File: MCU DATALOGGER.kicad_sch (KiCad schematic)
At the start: 0 parts

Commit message: Setup of EEschema for new project
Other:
- title: (none) -> MCU DATALOGGER
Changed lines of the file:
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@@
 	(generator_version "9.0")
 	(paper "A4")
+	(title_block
+		(title "MCU DATALOGGER")
+		(date "2026-05-03")
+		(rev "1")
+	)
 	(sheet_instances
 		(path "/"

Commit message: Have added required symbols to the schematic sheets
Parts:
- added BT1: Battery, symbol Device:Battery
- added C1, C2, C3, C4: C, symbol Device:C
- added C5: C_Polarized, symbol Device:C_Polarized
- added D1, D2: LED, symbol Device:LED
- added H1, H2, H3, H4, H5: MountingHole, symbol Mechanical:MountingHole
- added R1, R2, R3, R4, R5, R6, R7: R, symbol Device:R
- added U1, U2: 24LC1025, symbol Memory_EEPROM:24LC1025
- added U3: ATMEGA328P-AU, digikey-footprints:TQFP-32_7x7mm, symbol dk_Embedded-Microcontrollers:ATMEGA328P-AU
- added U4: DS1337S_, DS1337S_:SOIC127P600X175-8N, symbol DS1337S_:DS1337S_
- added Y1, Y2: Crystal, symbol Device:Crystal
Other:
- added sheet connectors (connectors.kicad_sch)

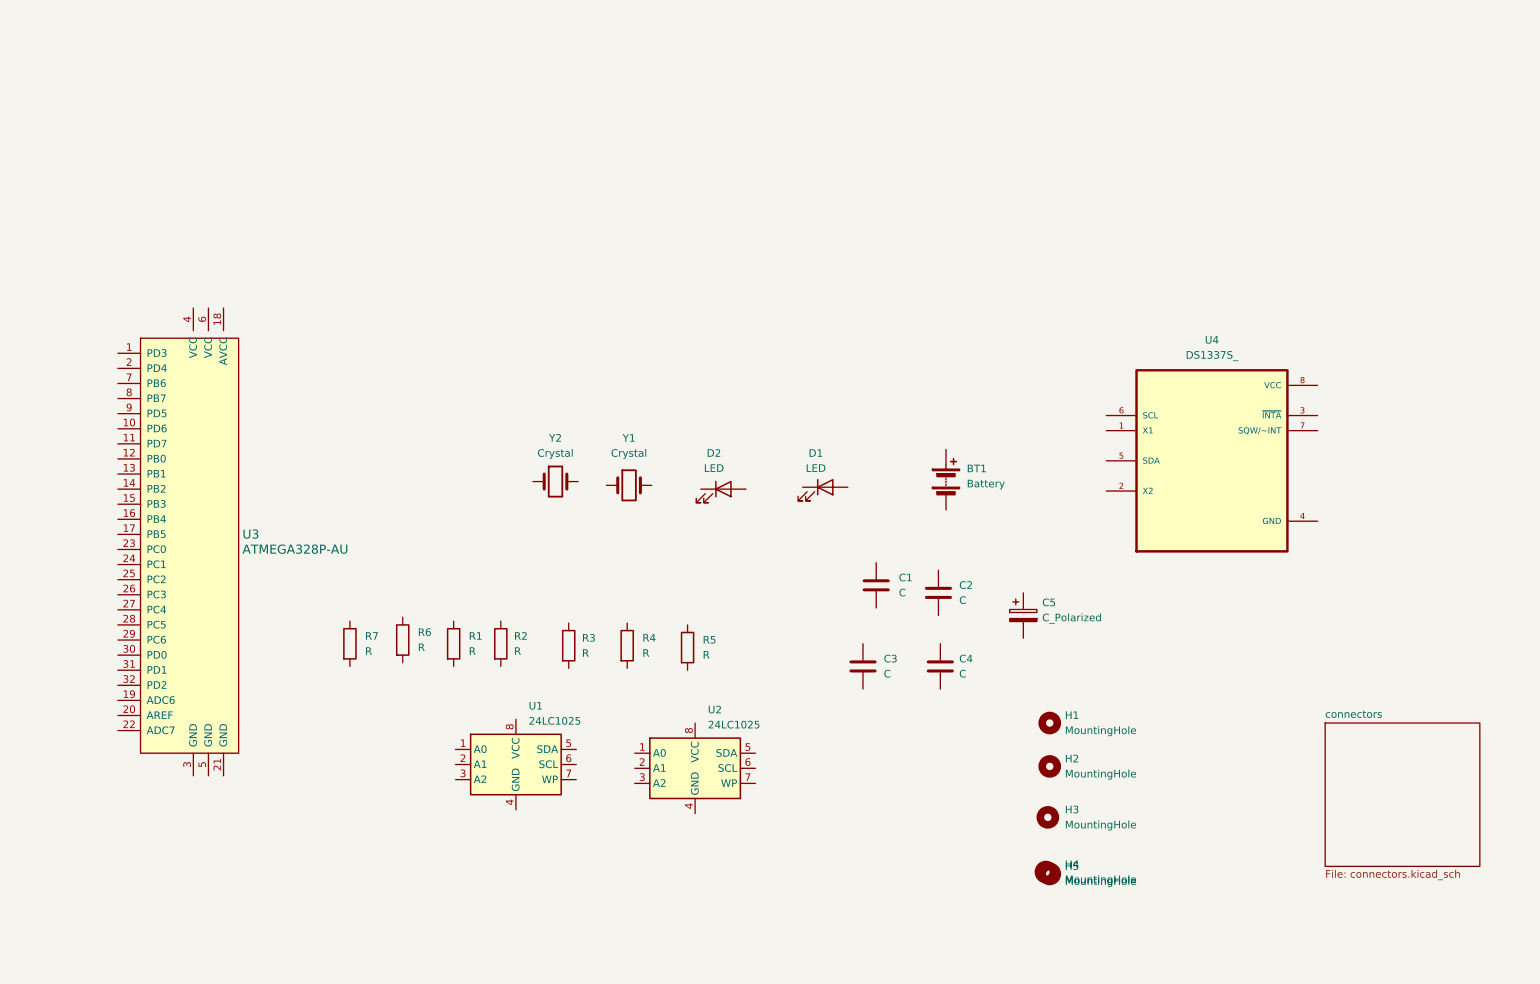
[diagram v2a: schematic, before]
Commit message: added values to symbols
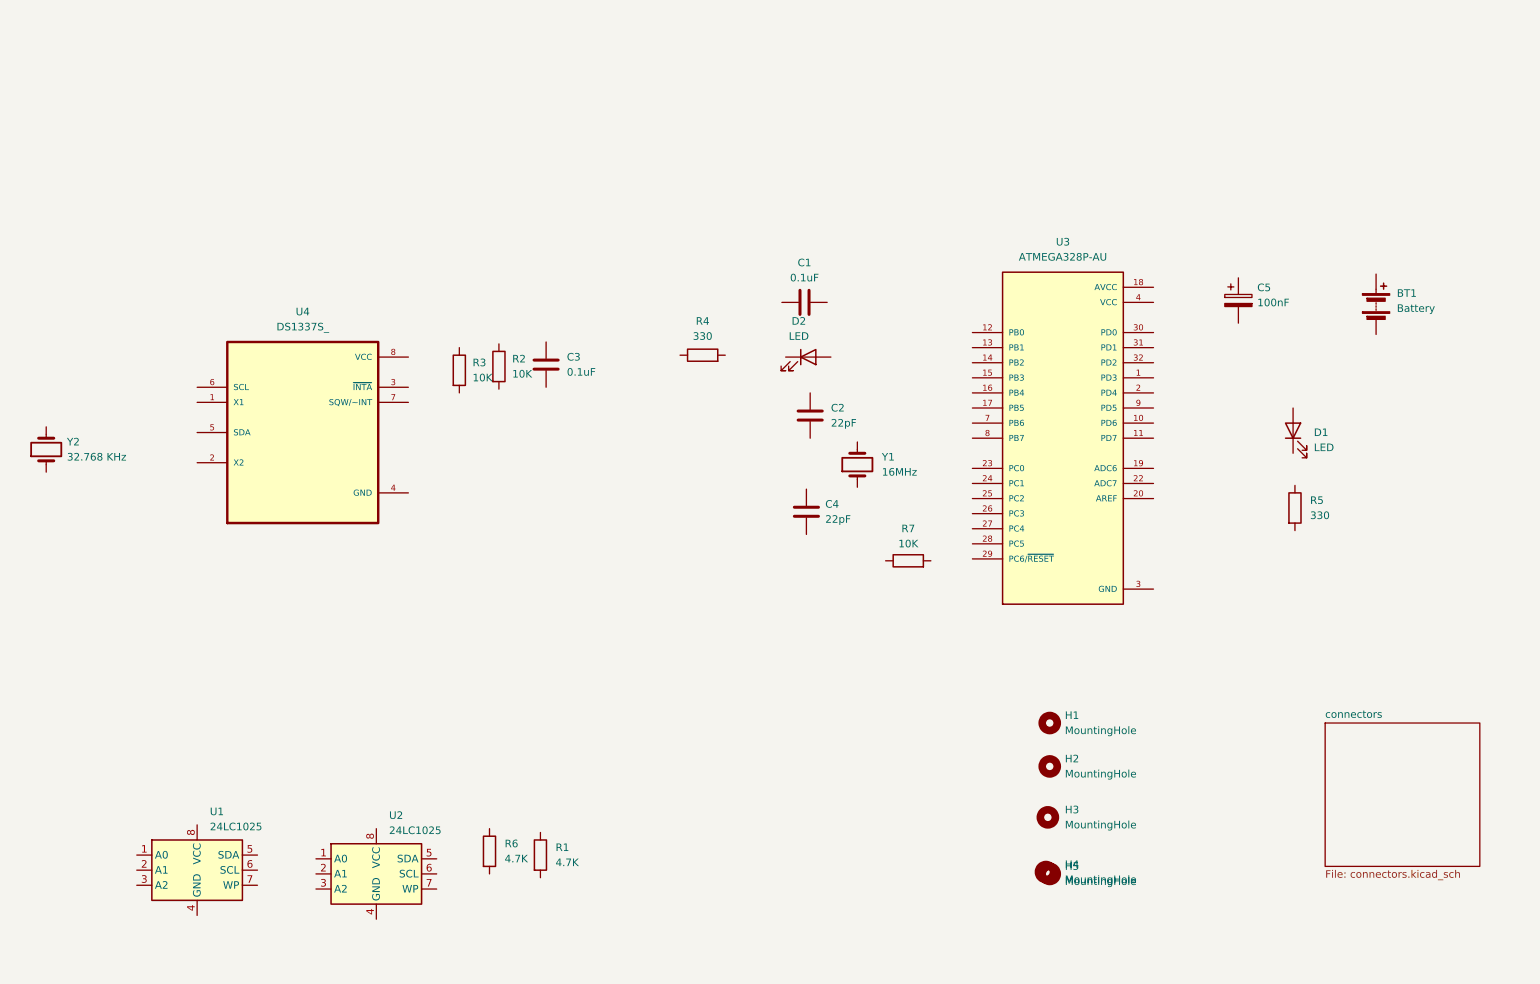
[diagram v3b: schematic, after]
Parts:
- removed U3: ATMEGA328P-AU, digikey-footprints:TQFP-32_7x7mm, symbol dk_Embedded-Microcontrollers:ATMEGA328P-AU
- added U3: ATMEGA328P-AU, ATMEGA328P-AU:QFP80P900X900X120-32N, symbol ATMEGA328P-AU:ATMEGA328P-AU
- C1, C3: value C -> 0.1uF
- C2, C4: value C -> 22pF
- C5: value C_Polarized -> 100nF
- R1, R6: value R -> 4.7K
- R2, R3, R7: value R -> 10K
- R4, R5: value R -> 330
- Y1: value Crystal -> 16MHz
- Y2: value Crystal -> 32.768 KHz
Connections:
- new net GND: U3.21 (GND), U3.3 (GND), U3.5 (GND)
- new net VCC: U3.4 (VCC), U3.6 (VCC)
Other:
- moved on the sheet: BT1, C1, C2, C3, C4, C5, D1, D2, R1, R2, R3, R4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

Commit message: assigned the footprints
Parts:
- BT1: footprint (none) -> Connector_PinHeader_2.54mm:PinHeader_1x02_P2.54mm_Vertical
- C1, C2, C3, C4, C5: footprint (none) -> Capacitor_SMD:C_0805_2012Metric
- D1, D2: footprint (none) -> LED_SMD:LED_0805_2012Metric
- H1, H2, H3, H4, H5: footprint (none) -> MountingHole:MountingHole_2.1mm
- R1, R2, R3, R4, R5, R6, R7: footprint (none) -> Resistor_SMD:R_0805_2012Metric
- U1, U2: footprint (none) -> Package_SO:SOIC-8_5.3x5.3mm_P1.27mm
- Y1, Y2: footprint (none) -> Crystal:Crystal_SMD_5032-2Pin_5.0x3.2mm_HandSoldering
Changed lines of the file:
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@@
 			)
 		)
-		(property "Footprint" ""
+		(property "Footprint" "LED_SMD:LED_0805_2012Metric"
 			(at 152.4 67.6275 0)
 			(effects
@@
 			)
 		)
-		(property "Footprint" ""
+		(property "Footprint" "MountingHole:MountingHole_2.1mm"
 			(at 193.04 129.2225 0)
 			(effects
@@
 			)
 		)
-		(property "Footprint" ""
+		(property "Footprint" "Connector_PinHeader_2.54mm:PinHeader_1x02_P2.54mm_Vertical"
 			(at 247.9675 57.2135 90)
 			(effects
@@
 			)
 		)
-		(property "Footprint" ""
+		(property "Footprint" "Resistor_SMD:R_0805_2012Metric"
 			(at 96.9645 150.8125 90)
 			(effects
@@
 			)
 		)
-		(property "Footprint" ""
+		(property "Footprint" "Resistor_SMD:R_0805_2012Metric"
 			(at 105.537 151.4475 90)
 			(effects
@@
 			)
 		)
-		(property "Footprint" ""
+		(property "Footprint" "Capacitor_SMD:C_0805_2012Metric"
 			(at 109.2327 72.7075 0)
 			(effects
@@
 			)
 		)
-		(property "Footprint" ""
+		(property "Footprint" "Capacitor_SMD:C_0805_2012Metric"
 			(at 225.7552 61.9125 0)
 			(effects
@@
 			)
 		)
-		(property "Footprint" ""
+		(property "Footprint" "Resistor_SMD:R_0805_2012Metric"
 			(at 169.2275 103.6955 90)
 			(effects
@@
 			)
 		)
-		(property "Footprint" ""
+		(property "Footprint" "Crystal:Crystal_SMD_5032-2Pin_5.0x3.2mm_HandSoldering"
 			(at 24.13 83.185 0)
 			(effects
@@
 			)
 		)
-		(property "Footprint" ""
+		(property "Footprint" "Crystal:Crystal_SMD_5032-2Pin_5.0x3.2mm_HandSoldering"
 			(at 160.655 85.725 0)
 			(effects
@@
 			)
 		)
-		(property "Footprint" ""
+		(property "Footprint" "Capacitor_SMD:C_0805_2012Metric"
 			(at 153.0477 97.4725 0)
 			(effects
@@
 			)
 		)
-		(property "Footprint" ""
+		(property "Footprint" "Capacitor_SMD:C_0805_2012Metric"
 			(at 155.575 57.4548 0)
 			(effects
@@
 			)
 		)
-		(property "Footprint" ""
+		(property "Footprint" "MountingHole:MountingHole_2.1mm"
 			(at 193.04 154.6225 0)
 			(effects
@@
 			)
 		)
-		(property "Footprint" ""
+		(property "Footprint" "Capacitor_SMD:C_0805_2012Metric"
 			(at 153.6827 81.28 0)
 			(effects
@@
 			)
 		)
-		(property "Footprint" ""
+		(property "Footprint" "MountingHole:MountingHole_2.1mm"
 			(at 193.04 136.525 0)
 			(effects
@@
 			)
 		)
-		(property "Footprint" ""
+		(property "Footprint" "MountingHole:MountingHole_2.1mm"
 			(at 192.405 154.305 0)
 			(effects
@@
 			)
 		)
-		(property "Footprint" ""
+		(property "Footprint" "Resistor_SMD:R_0805_2012Metric"
 			(at 134.62 69.088 90)
 			(effects
@@
 			)
 		)
-		(property "Footprint" ""
+		(property "Footprint" "MountingHole:MountingHole_2.1mm"
 			(at 192.7225 145.0975 0)
 			(effects
@@
 			)
 		)
-		(property "Footprint" ""
+		(property "Footprint" "Package_SO:SOIC-8_5.3x5.3mm_P1.27mm"
 			(at 79.6925 154.6225 0)
 			(effects
@@
 			)
 		)
-		(property "Footprint" ""
+		(property "Footprint" "Package_SO:SOIC-8_5.3x5.3mm_P1.27mm"
 			(at 49.53 153.9875 0)
 			(effects
@@
 			)
 		)
-		(property "Footprint" ""
+		(property "Footprint" "Resistor_SMD:R_0805_2012Metric"
 			(at 98.552 69.215 90)
 			(effects
@@
 			)
 		)
-		(property "Footprint" ""
+		(property "Footprint" "LED_SMD:LED_0805_2012Metric"
 			(at 233.9975 80.01 0)
 			(effects
@@
 			)
 		)
-		(property "Footprint" ""
+		(property "Footprint" "Resistor_SMD:R_0805_2012Metric"
 			(at 232.537 93.0275 90)
 			(effects
@@
 			)
 		)
-		(property "Footprint" ""
+		(property "Footprint" "Resistor_SMD:R_0805_2012Metric"
 			(at 91.8845 69.85 90)
 			(effects

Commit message: done wiring of the main sheet
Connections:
- net GND: now also BT1.2 (-), C1.2, C2.1, C3.2, C4.1, C5.2, R4.1, U1.4 (GND), U2.2 (A1), U2.4 (GND), U4.4 (GND)
- net VCC: now also C3.1, R1.1, R2.1, R3.1, R6.1, R7.1, U1.1 (A0), U1.2 (A1), U1.3 (A2), U1.8 (VCC), U2.1 (A0), U2.3 (A2), U2.8 (VCC), U4.8 (VCC); no longer U3.4 (VCC), U3.6 (VCC)
- net at D2.1 (K): now also R4.2
- net at D2.2 (A): now also U3.17 (PB5)
- net at BT1.1 (+): now also C5.1, D1.2 (A), U3.18 (AVCC), U3.6 (VCC)
- net SCK: now reaches R6.2
- net SCK: now also U1.6 (SCL), U2.6 (SCL), U3.28 (PC5), U4.6 (SCL)
- net SDA: now reaches R1.2
- net SDA: now also U1.5 (SDA), U2.5 (SDA), U3.27 (PC4), U4.5 (SDA)
- net at U4.1 (X1): now also Y2.2
- net at U4.2 (X2): now also Y2.1
- net at U4.3 (~{INTA}): now also R3.2
- net at U4.7 (SQW/~INT): now also R2.2
- net RESET: now reaches R7.2
- net RESET: now also U3.29 (PC6/~{RESET})
- net at Y1.1: now also C4.2, U3.8 (PB7)
- net at Y1.2: now also C2.2, U3.7 (PB6)
- net at C1.1: now also U3.20 (AREF)
- net D3: now reaches U3.1 (PD3)
- net D6: now reaches U3.10 (PD6)
- net D7: now reaches U3.11 (PD7)
- net D8: now reaches U3.12 (PB0)
- net MOSI: now reaches U3.15 (PB3)
- net MISO: now reaches U3.16 (PB4)
- net D4: now reaches U3.2 (PD4)
- net RX: now reaches U3.30 (PD0)
- net TX: now reaches U3.31 (PD1)
- net D2: now reaches U3.32 (PD2)
- net D5: now reaches U3.9 (PD5)
- net at D1.1 (K): now also R5.1
- no-connect marks 0 -> 8
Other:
- moved on the sheet: BT1, C1, C2, C3, C4, C5, D1, D2, R2, R3, R4, R5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

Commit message: Completed all the wiring
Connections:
- net GND: now also R5.2, U1.7 (WP), U2.7 (WP)
- net SCK: now also D2.2 (A), U3.17 (PB5)
- no-connect marks 8 -> 9
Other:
- sheet connectors ports: added D2, D3, D4, D5, D6, D7, D8, GND, MISO, MOSI, RESET, RX, SCK, SDA, TX, VCC; removed none
- moved on the sheet: H1, H2, H3, H4, H5

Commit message: Done with schematic
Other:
- note added: "EEPROM"
- note added: "MCU"
- note added: "MOUNTING"
- note added: "REAL TIME CLOCK"
- moved on the sheet: BT1, C1, C2, C3, C4, C5, D1, D2, R2, R3, R4, R5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

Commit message: Imported the parts and set the settings
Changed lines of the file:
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@@
 		(at 197.1675 72.0725)
+	)
+	(bus_entry
+		(at 63.8175 9.525)
+		(size 2.54 2.54)
+		(stroke
+			(width 0)
+			(type default)
+		)
 	)
 	(wire
